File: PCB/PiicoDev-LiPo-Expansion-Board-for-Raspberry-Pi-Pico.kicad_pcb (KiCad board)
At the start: 2 copper layers, 50.4 x 51.4 mm, 26 parts, among them J1 PiicoDev, J2 JST PH, J3 , J4 , Q1 DMG3415U-7, U1 MCP73832-2-OT

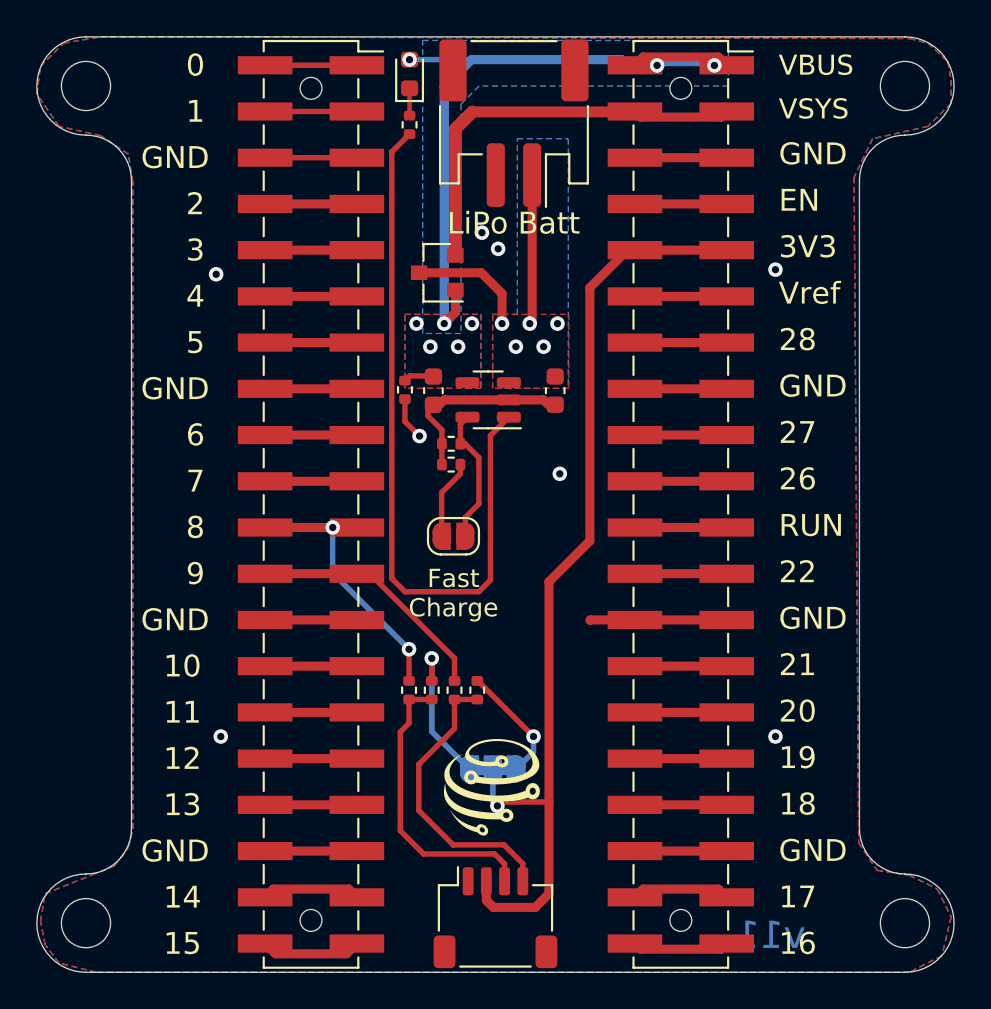
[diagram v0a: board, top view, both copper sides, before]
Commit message: update artwork for 'LiPo' expansion
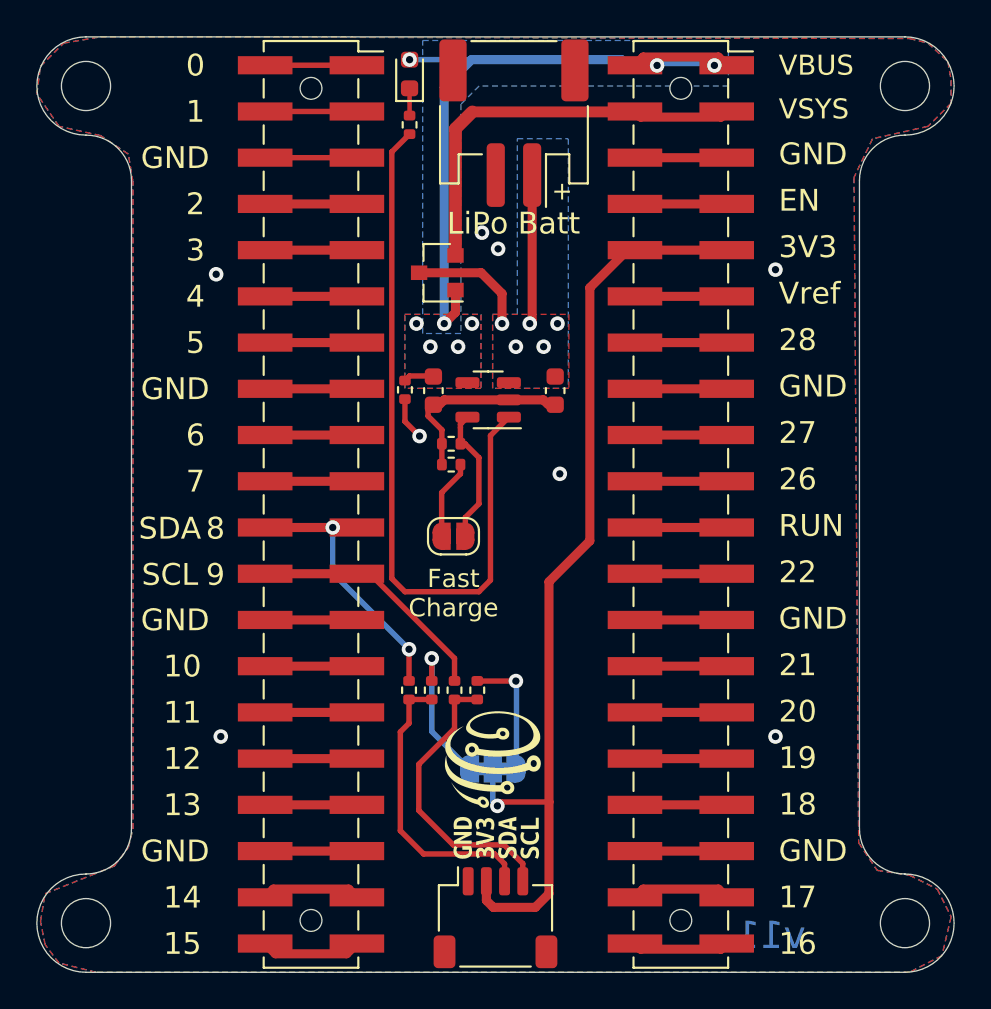
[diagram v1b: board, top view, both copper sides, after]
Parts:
- removed G***: LOGO, CoreElectronics_Artwork:CoreElectronics_logo_5mm
- added kibuzzard-629D8D51: G***, kibuzzard-629D8D51, F.Cu at (23.2, 44.0)
- added kibuzzard-629D8D5D: G***, kibuzzard-629D8D5D, F.Cu at (24.4, 44.0)
- added kibuzzard-629D8D64: G***, kibuzzard-629D8D64, F.Cu at (25.7, 44.0)
- added kibuzzard-629D8D6F: G***, kibuzzard-629D8D6F, F.Cu at (26.9, 44.0)
- added kibuzzard-629D9090: G***, kibuzzard-629D9090, B.Cu at (21.8, 13.6)
- added kibuzzard-629D909F: G***, kibuzzard-629D909F, B.Cu at (25.0, 18.6)
- added kibuzzard-629D90AA: G***, kibuzzard-629D90AA, B.Cu at (25.0, 21.3)
- added kibuzzard-62DE0FE6: G***, kibuzzard-62DE0FE6, B.Cu at (34.8, 13.3)
- moved G1 1.52 mm to (24.9, 39.7)
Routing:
- net GND: track 56.6 -> 54.1 mm
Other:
- net class Default removed
- net class Generous removed
- board text added: "+"
- board text added: "SCL"
- board text added: "SDA"
- board text removed: "Expansion Board for Raspberry Pi Pico"
